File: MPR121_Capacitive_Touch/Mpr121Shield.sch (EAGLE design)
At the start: 13 parts

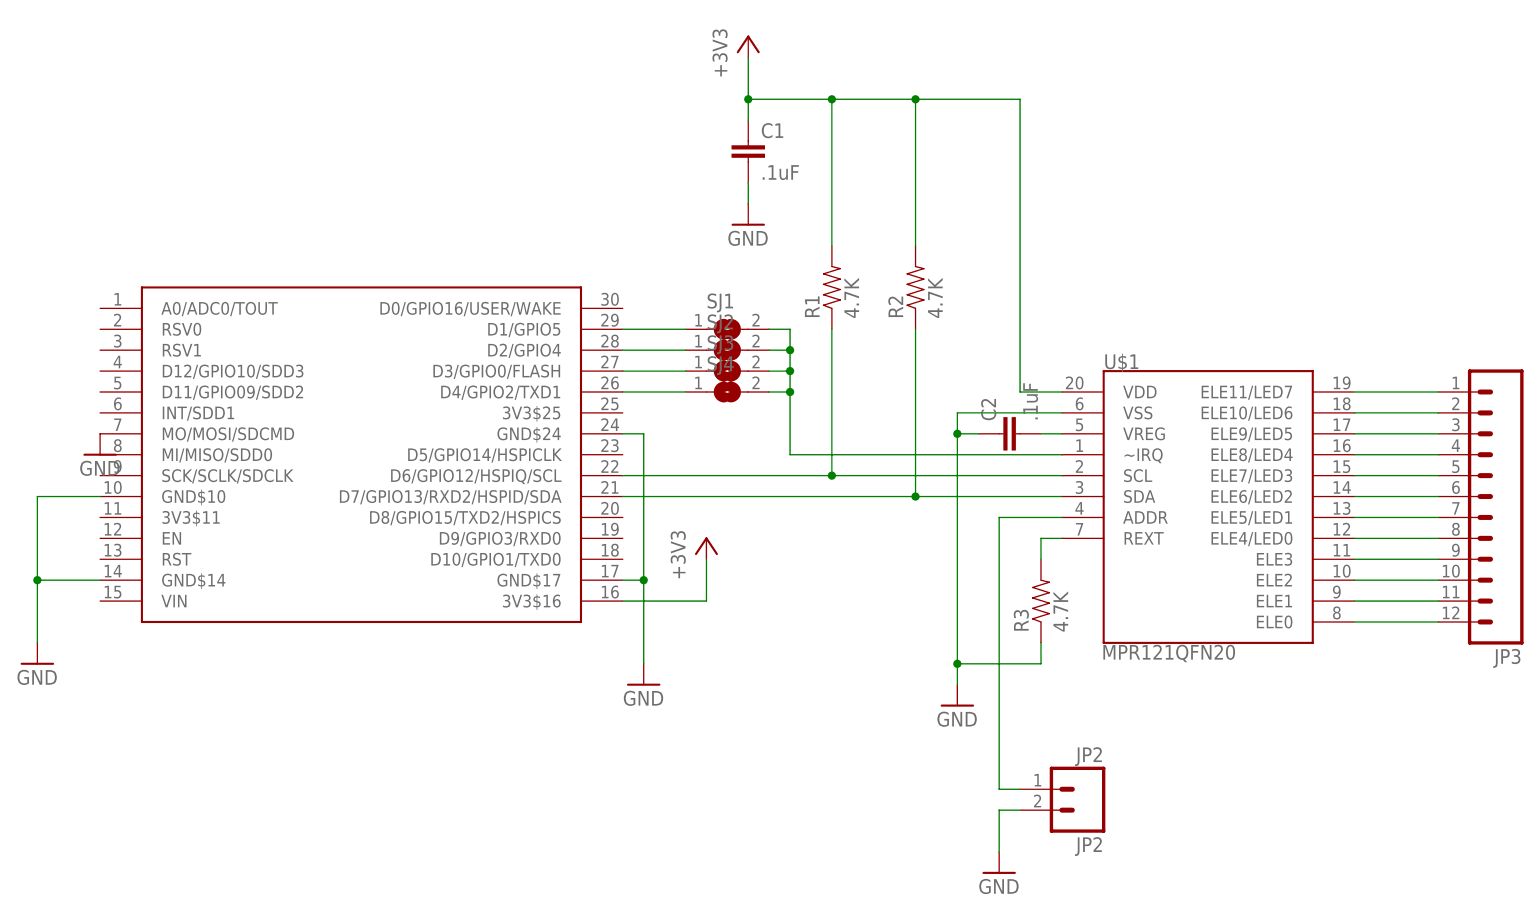
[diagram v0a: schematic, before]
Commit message: Added OLED Shield Added LiPo Battery Charger Shield Updated outlines of all shields to match the cutout of the nodemcu board
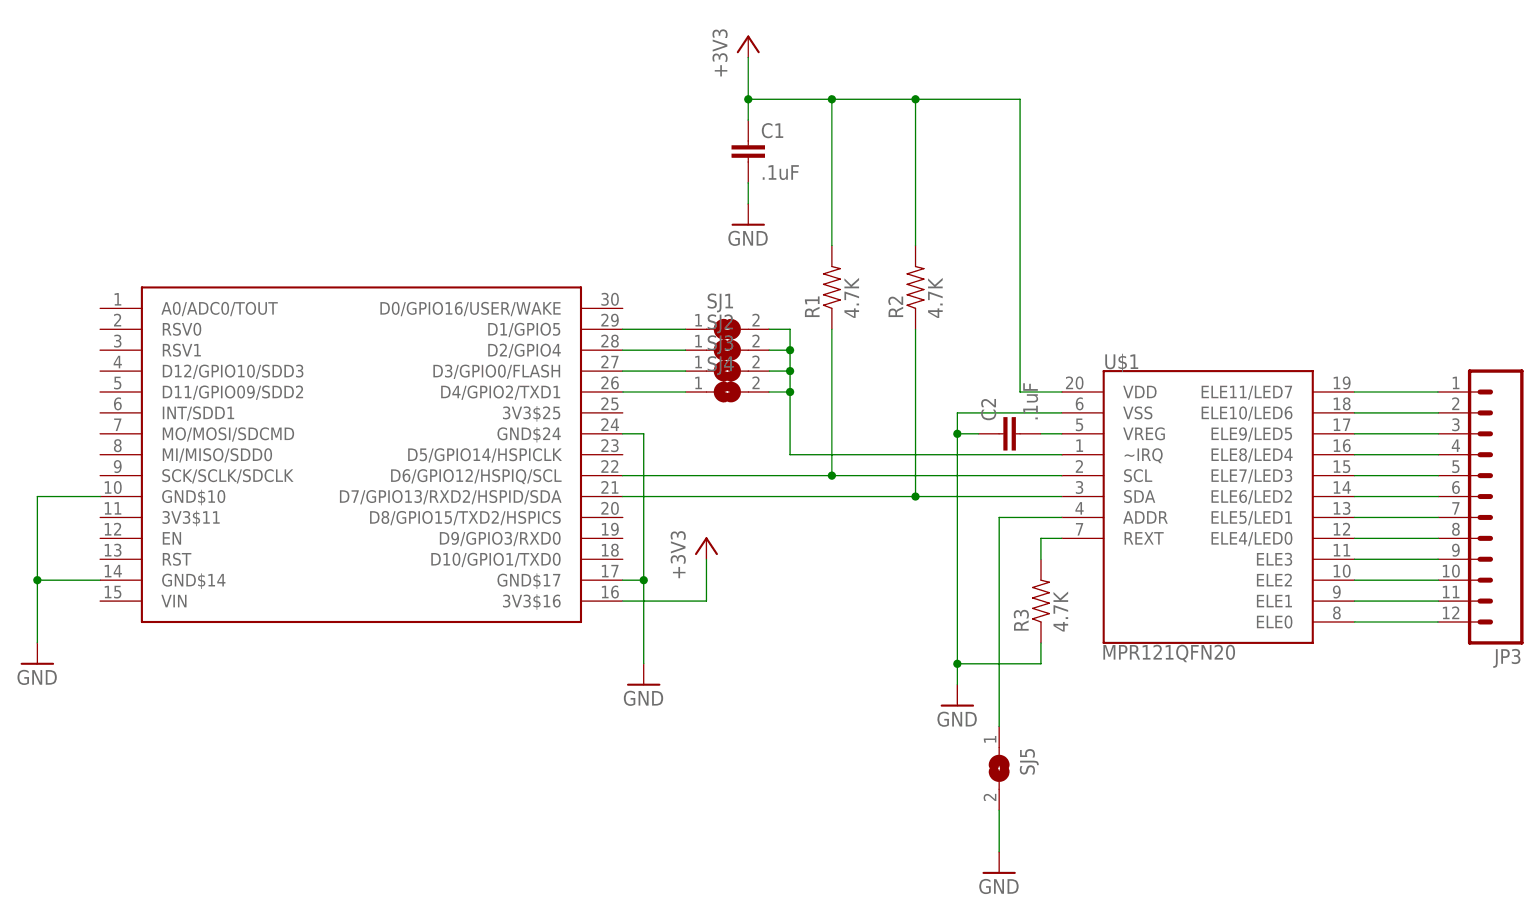
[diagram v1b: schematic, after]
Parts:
- removed JP2: JP2, SparkFun:M02PTH
- added SJ5: (no value), jumper:SJ
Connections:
- net GND: now also SJ5.2; no longer JP2.2, U$2.MO/MOSI/SDCMD
- net N$18: now also SJ5.1; no longer JP2.1
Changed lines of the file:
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@@
 <?xml version="1.0" encoding="utf-8"?>
 <!DOCTYPE eagle SYSTEM "eagle.dtd">
-<eagle version="7.3.0">
+<eagle version="7.4.0">
 <drawing>
 <settings>
@@
 </classes>
 <parts>
-<part name="GND2" library="SparkFun" deviceset="GND" device=""/>
 <part name="GND4" library="SparkFun" deviceset="GND" device=""/>
 <part name="C1" library="SparkFun" deviceset="CAP" device="0603-CAP" value=".1uF"/>
@@
 <part name="R2" library="SparkFun" deviceset="RESISTOR" device="0603-RES" value="4.7K"/>
 <part name="+3V2" library="supply1" deviceset="+3V3" device=""/>
-<part name="JP2" library="SparkFun" deviceset="M02" device="PTH" value="JP2"/>
 <part name="U$2" library="NerduinoShieldLib" deviceset="NERDSHIELD" device=""/>
 <part name="+3V1" library="supply1" deviceset="+3V3" device=""/>
@@
 <part name="SJ3" library="jumper" deviceset="SJ" device=""/>
 <part name="SJ4" library="jumper" deviceset="SJ" device=""/>
+<part name="SJ5" library="jumper" deviceset="SJ" device=""/>
 </parts>
 <sheets>
@@
 </plain>
 <instances>
-<instance part="GND2" gate="1" x="10.16" y="53.34"/>
 <instance part="GND4" gate="1" x="88.9" y="81.28"/>
 <instance part="C1" gate="G$1" x="88.9" y="88.9"/>
@@
 <instance part="R2" gate="G$1" x="109.22" y="73.66" rot="R90"/>
 <instance part="+3V2" gate="G$1" x="88.9" y="104.14"/>
-<instance part="JP2" gate="G$1" x="129.54" y="12.7" rot="R180"/>
 <instance part="U$2" gate="G$1" x="27.94" y="53.34"/>
 <instance part="+3V1" gate="G$1" x="83.82" y="43.18"/>
@@
 <instance part="SJ3" gate="1" x="86.36" y="63.5"/>
 <instance part="SJ4" gate="1" x="86.36" y="60.96"/>
+<instance part="SJ5" gate="1" x="119.38" y="15.24" rot="R270"/>
 </instances>
 <busses>
@@
 <pinref part="GND4" gate="1" pin="GND"/>
 <pinref part="C1" gate="G$1" pin="2"/>
-</segment>
-<segment>
-<pinref part="GND2" gate="1" pin="GND"/>
-<pinref part="U$2" gate="G$1" pin="MO/MOSI/SDCMD"/>
 </segment>
 <segment>
@@
 </segment>
 <segment>
-<pinref part="JP2" gate="G$1" pin="2"/>
 <pinref part="GND7" gate="1" pin="GND"/>
-<wire x1="121.92" y1="10.16" x2="119.38" y2="10.16" width="0.1524" layer="91"/>
 <wire x1="119.38" y1="10.16" x2="119.38" y2="5.08" width="0.1524" layer="91"/>
+<pinref part="SJ5" gate="1" pin="2"/>
 </segment>
 </net>
@@
 <pinref part="U$1" gate="G$1" pin="ADDR"/>
 <wire x1="127" y1="45.72" x2="119.38" y2="45.72" width="0.1524" layer="91"/>
-<wire x1="119.38" y1="45.72" x2="119.38" y2="12.7" width="0.1524" layer="91"/>
-<pinref part="JP2" gate="G$1" pin="1"/>
-<wire x1="121.92" y1="12.7" x2="119.38" y2="12.7" width="0.1524" layer="91"/>
-</segment>
-</net>
+<wire x1="119.38" y1="45.72" x2="119.38" y2="20.32" width="0.1524" layer="91"/>
+<pinref part="SJ5" gate="1" pin="1"/>
+</segment>
+</net>

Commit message: Updated the i2c pins to all shields to use d11/d12  as these pins will have dual use with the upcoming wifimcu Added FM24W256  Fram shield Added X95840 Digital potentiometer Shield Added AD5696 DAC Shield
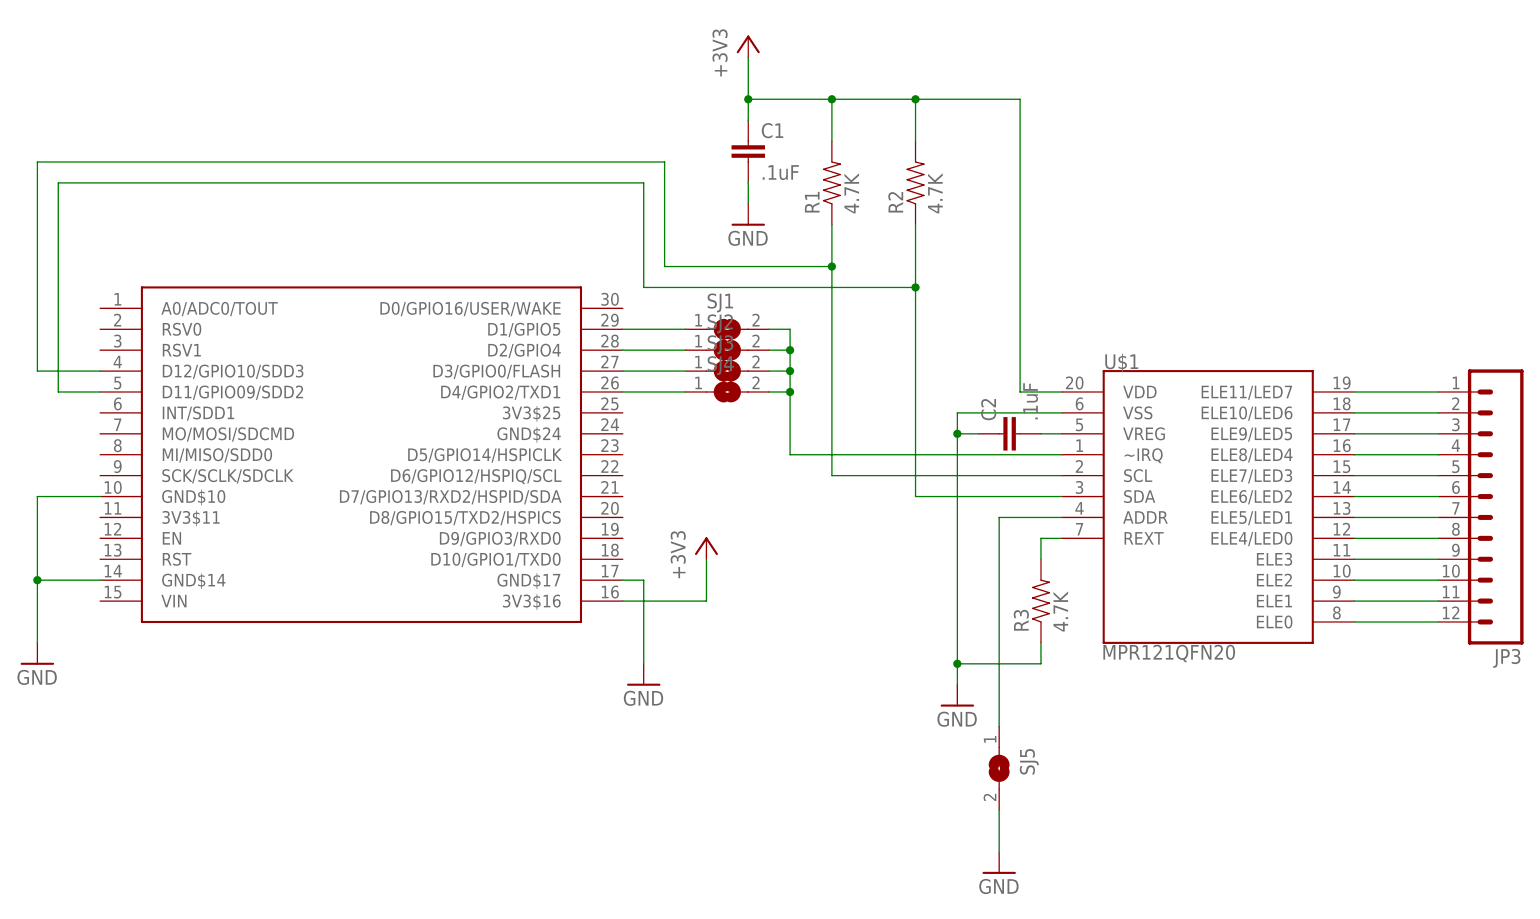
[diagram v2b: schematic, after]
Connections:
- net GND: no longer U$2.GND$24
- net N$2: now also U$2.D12/GPIO10/SDD3; no longer U$2.D6/GPIO12/HSPIQ/SCL
- net N$4: now also U$2.D11/GPIO09/SDD2; no longer U$2.D7/GPIO13/RXD2/HSPID/SDA
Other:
- moved on the sheet: R1, R2
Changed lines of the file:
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@@
 <instance part="GND4" gate="1" x="88.9" y="81.28"/>
 <instance part="C1" gate="G$1" x="88.9" y="88.9"/>
-<instance part="R1" gate="G$1" x="99.06" y="73.66" rot="R90"/>
-<instance part="R2" gate="G$1" x="109.22" y="73.66" rot="R90"/>
+<instance part="R1" gate="G$1" x="99.06" y="86.36" rot="R90"/>
+<instance part="R2" gate="G$1" x="109.22" y="86.36" rot="R90"/>
 <instance part="+3V2" gate="G$1" x="88.9" y="104.14"/>
 <instance part="U$2" gate="G$1" x="27.94" y="53.34"/>
@@
 <pinref part="GND6" gate="1" pin="GND"/>
 <wire x1="76.2" y1="27.94" x2="76.2" y2="38.1" width="0.1524" layer="91"/>
-<pinref part="U$2" gate="G$1" pin="GND$24"/>
-<wire x1="76.2" y1="38.1" x2="76.2" y2="55.88" width="0.1524" layer="91"/>
-<wire x1="76.2" y1="55.88" x2="73.66" y2="55.88" width="0.1524" layer="91"/>
 <pinref part="U$2" gate="G$1" pin="GND$17"/>
 <wire x1="73.66" y1="38.1" x2="76.2" y2="38.1" width="0.1524" layer="91"/>
-<junction x="76.2" y="38.1"/>
 </segment>
 <segment>
@@
 <wire x1="88.9" y1="101.6" x2="88.9" y2="96.52" width="0.1524" layer="91"/>
 <wire x1="88.9" y1="96.52" x2="99.06" y2="96.52" width="0.1524" layer="91"/>
-<wire x1="99.06" y1="78.74" x2="99.06" y2="96.52" width="0.1524" layer="91"/>
+<wire x1="99.06" y1="91.44" x2="99.06" y2="96.52" width="0.1524" layer="91"/>
 <wire x1="99.06" y1="96.52" x2="109.22" y2="96.52" width="0.1524" layer="91"/>
-<wire x1="109.22" y1="78.74" x2="109.22" y2="96.52" width="0.1524" layer="91"/>
+<wire x1="109.22" y1="91.44" x2="109.22" y2="96.52" width="0.1524" layer="91"/>
 <junction x="88.9" y="96.52"/>
 <junction x="99.06" y="96.52"/>
@@
 <net name="N$2" class="0">
 <segment>
-<pinref part="U$2" gate="G$1" pin="D6/GPIO12/HSPIQ/SCL"/>
-<wire x1="73.66" y1="50.8" x2="99.06" y2="50.8" width="0.1524" layer="91"/>
 <pinref part="U$1" gate="G$1" pin="SCL"/>
 <pinref part="R1" gate="G$1" pin="1"/>
 <wire x1="99.06" y1="50.8" x2="127" y2="50.8" width="0.1524" layer="91"/>
-<wire x1="99.06" y1="68.58" x2="99.06" y2="50.8" width="0.1524" layer="91"/>
-<junction x="99.06" y="50.8"/>
+<wire x1="99.06" y1="81.28" x2="99.06" y2="76.2" width="0.1524" layer="91"/>
+<wire x1="99.06" y1="76.2" x2="99.06" y2="50.8" width="0.1524" layer="91"/>
+<wire x1="99.06" y1="76.2" x2="78.74" y2="76.2" width="0.1524" layer="91"/>
+<wire x1="78.74" y1="76.2" x2="78.74" y2="88.9" width="0.1524" layer="91"/>
+<junction x="99.06" y="76.2"/>
+<wire x1="78.74" y1="88.9" x2="2.54" y2="88.9" width="0.1524" layer="91"/>
+<wire x1="2.54" y1="88.9" x2="2.54" y2="63.5" width="0.1524" layer="91"/>
+<pinref part="U$2" gate="G$1" pin="D12/GPIO10/SDD3"/>
+<wire x1="2.54" y1="63.5" x2="10.16" y2="63.5" width="0.1524" layer="91"/>
 </segment>
 </net>
 <net name="N$4" class="0">
 <segment>
-<pinref part="U$2" gate="G$1" pin="D7/GPIO13/RXD2/HSPID/SDA"/>
 <pinref part="U$1" gate="G$1" pin="SDA"/>
-<wire x1="73.66" y1="48.26" x2="109.22" y2="48.26" width="0.1524" layer="91"/>
 <pinref part="R2" gate="G$1" pin="1"/>
 <wire x1="109.22" y1="48.26" x2="127" y2="48.26" width="0.1524" layer="91"/>
-<wire x1="109.22" y1="68.58" x2="109.22" y2="48.26" width="0.1524" layer="91"/>
-<junction x="109.22" y="48.26"/>
+<wire x1="109.22" y1="81.28" x2="109.22" y2="73.66" width="0.1524" layer="91"/>
+<wire x1="109.22" y1="73.66" x2="109.22" y2="48.26" width="0.1524" layer="91"/>
+<wire x1="109.22" y1="73.66" x2="76.2" y2="73.66" width="0.1524" layer="91"/>
+<wire x1="76.2" y1="73.66" x2="76.2" y2="86.36" width="0.1524" layer="91"/>
+<junction x="109.22" y="73.66"/>
+<wire x1="76.2" y1="86.36" x2="5.08" y2="86.36" width="0.1524" layer="91"/>
+<wire x1="5.08" y1="86.36" x2="5.08" y2="60.96" width="0.1524" layer="91"/>
+<pinref part="U$2" gate="G$1" pin="D11/GPIO09/SDD2"/>
+<wire x1="5.08" y1="60.96" x2="10.16" y2="60.96" width="0.1524" layer="91"/>
 </segment>
 </net>
